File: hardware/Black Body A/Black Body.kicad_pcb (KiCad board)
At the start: 2 copper layers, 52 x 53.8 mm, 36 parts, among them IC2 MCP96L00T-E_MX, J1 53307-2471, J2 Conn_01x02, J3 Conn_01x04, J5 Conn_02x04_Top_Bottom, J7 Conn_02x03_Top_Bottom

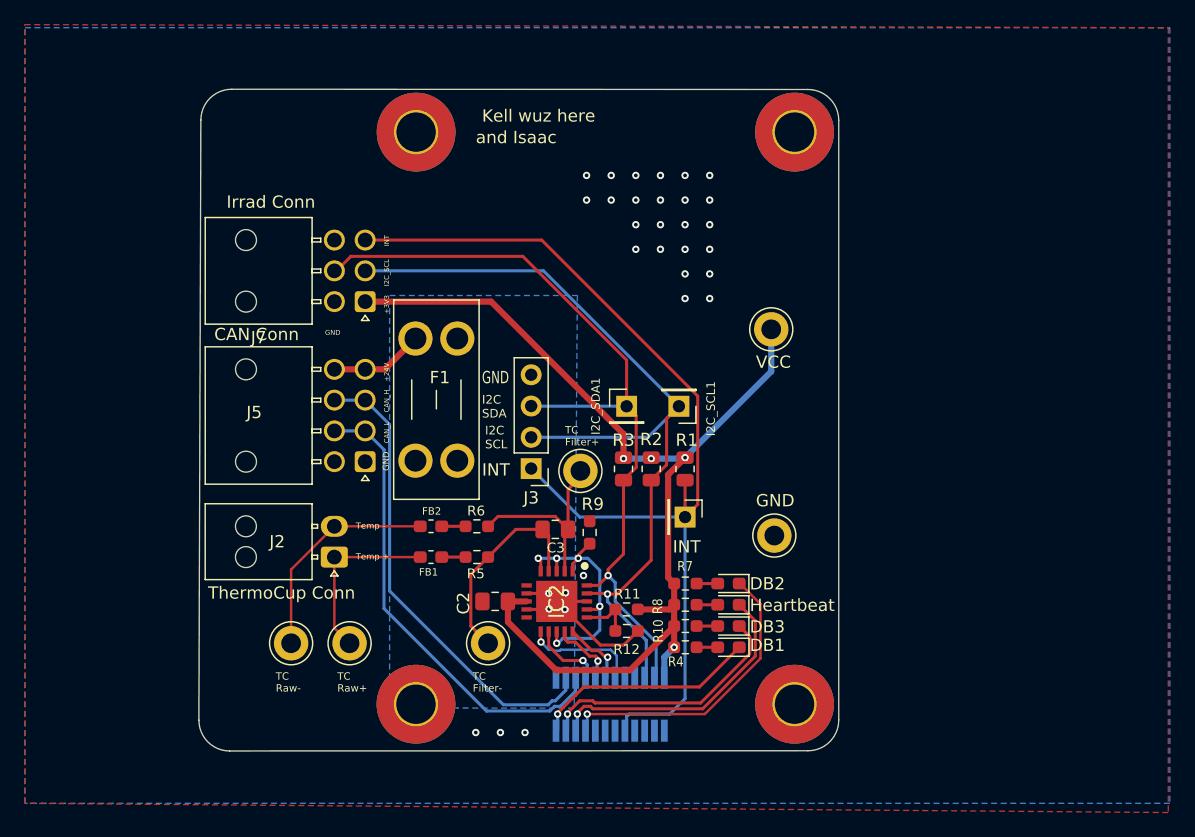
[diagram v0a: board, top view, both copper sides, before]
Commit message: updated irrad board layout + removed testpoints
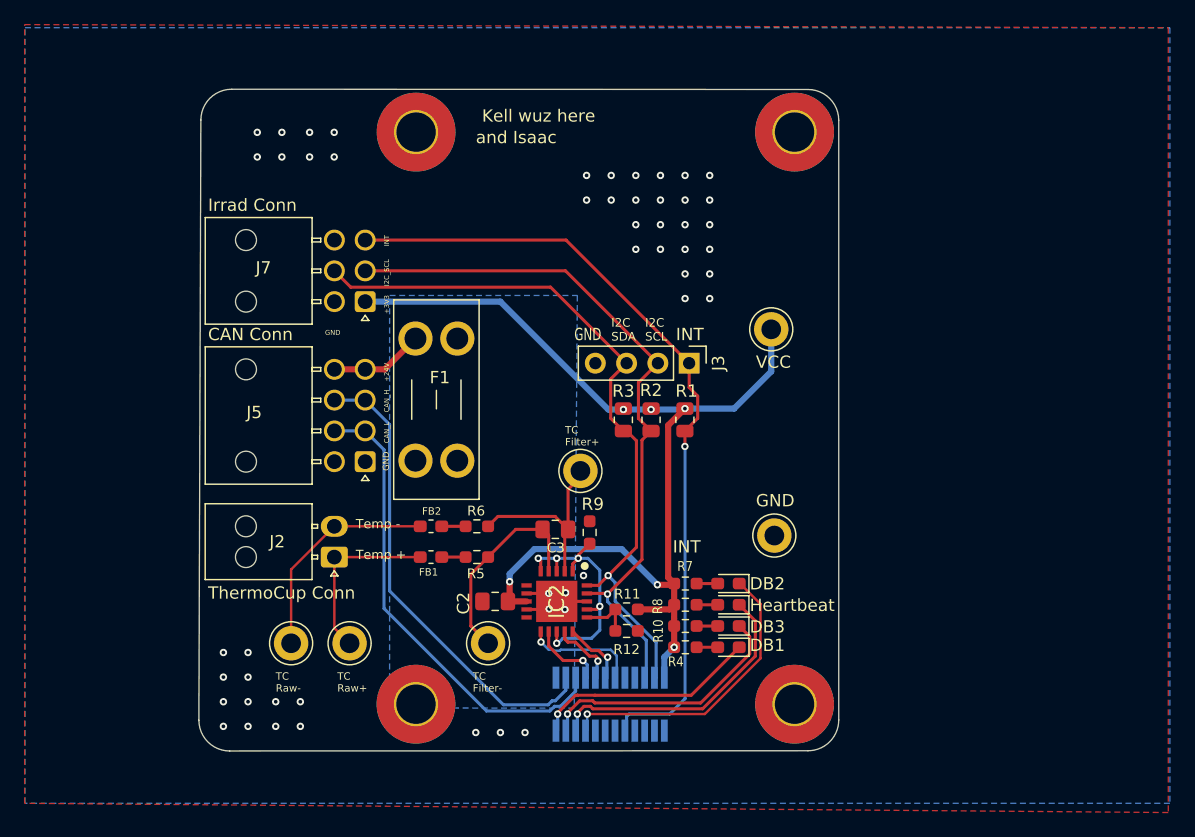
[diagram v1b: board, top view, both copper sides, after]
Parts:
- removed I2C_SCL1, I2C_SDA1, INT1: TestPoint, Connector_PinHeader_2.54mm:PinHeader_1x01_P2.54mm_Vertical
- moved J3 15.4 mm to (117.3, 89.2), turned to -90 degrees
- moved R1 3.99 mm to (117.0, 93.9)
- moved R2 3.99 mm to (114.2, 93.9)
- moved R3 3.99 mm to (112.0, 93.9)
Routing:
- net /INT: track 80.9 -> 64.9 mm, vias 0 -> 1
- net /I2C1_SCL: track 71.6 -> 58.0 mm
- net /I2C1_SDA: track 66.8 -> 59.0 mm
- net GND: track 15.8 -> 8.22 mm, vias 32 -> 52
- net +3V3: track 87.6 -> 86.6 mm, vias 4 -> 6

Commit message: updated 24Va
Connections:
- F2 pad 1: +24V -> /+24V_Ext
- J5 pad 1: +24V -> /+24V_Ext
- J5 pad 5: +24V -> /+24V_Ext
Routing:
- net +24V: track 7.62 -> 0.00 mm
- net GND: track 8.22 -> 14.3 mm, vias 52 -> 51
- added copper zone on B.Cu, net /+24V_Ext
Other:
- board text added: "and Isaac and Aarav and Frank"
- board text removed: "and Isaac"
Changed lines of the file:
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@@
 	(net 46 "/Temp-")
 	(net 47 "unconnected-(J7-Pin_6-Pad6)")
+	(net 48 "/+24V_Ext")
 	(footprint "Resistor_SMD:R_0603_1608Metric_Pad0.98x0.95mm_HandSolder"
 		(layer "F.Cu")
@@
 			(layers "*.Cu" "*.Mask")
 			(remove_unused_layers no)
-			(net 40 "+24V")
+			(net 48 "/+24V_Ext")
 			(pintype "passive")
 		)
@@
 			(layers "*.Cu" "*.Mask")
 			(remove_unused_layers no)
-			(net 40 "+24V")
+			(net 48 "/+24V_Ext")
 			(pintype "passive")
 		)
@@
 			(layers "*.Cu" "*.Mask")
 			(remove_unused_layers no)
-			(net 40 "+24V")
+			(net 48 "/+24V_Ext")
 			(pinfunction "Pin_1")
 			(pintype "passive")
@@
 			(layers "*.Cu" "*.Mask")
 			(remove_unused_layers no)
-			(net 40 "+24V")
+			(net 48 "/+24V_Ext")
 			(pinfunction "Pin_5")
 			(pintype "passive")
@@
 		)
 	)
-	(gr_text "and Isaac"
-		(at 100 71.5 0)
+	(gr_text "and Isaac and Aarav and Frank"
+		(at 100.1 71.6 0)
 		(layer "F.SilkS")
 		(effects
 			(font
-				(size 1 1)
+				(size 1 0.75)
 				(thickness 0.15)
 			)
@@
 		)
 	)
-	(gr_text "DB2"
-		(at 122.25 107.75 0)
+	(gr_text "DB1"
+		(at 122.3 107.8 0)
 		(layer "F.SilkS")
 		(effects
@@
 		)
 	)
-	(gr_text "DB3"
+	(gr_text "DB2"
 		(at 122.25 111.25 0)
 		(layer "F.SilkS")
@@
 	)
 	(gr_text "Kell wuz here"
-		(at 100.5 69.75 0)
+		(at 100.2 70.1 0)
 		(layer "F.SilkS")
 		(effects
@@
 		)
 	)
-	(gr_text "DB1\n"
+	(gr_text "DB3\n"
 		(at 122.25 112.75 0)
 		(layer "F.SilkS")
@@
 		)
 	)
-	(gr_text "INT"
-		(at 116 104.75 0)
-		(layer "F.SilkS")
-		(effects
-			(font
-				(size 1 1)
-				(thickness 0.1)
-			)
-			(justify left bottom)
-		)
-	)
 	(gr_text "I2C_SCL\n"
 		(at 93 83 90)
@@
 		(effects
 			(font
-				(size 1 1)
+				(size 1 0.75)
 				(thickness 0.15)
 			)
@@
 	)
 	(segment
+		(start 106.6 108.6)
+		(end 108.75 110.75)
+		(width 0.25)
+		(layer "F.Cu")
+		(net 1)
+	)
+	(segment
+		(start 106.575 108.6)
+		(end 106.65 108.6)
+		(width 0.25)
+		(layer "F.Cu")
+		(net 1)
+	)
+	(segment
 		(start 104.125 109.25)
 		(end 105.925 109.25)
@@
 	)
 	(segment
+		(start 106.65 108.6)
+		(end 108.75 106.5)
+		(width 0.25)
+		(layer "F.Cu")
+		(net 1)
+	)
+	(segment
 		(start 106.575 108.6)
 		(end 106.6 108.6)
@@
 	)
 	(via
-		(at 108.75 106.5)
-		(size 0.6)
-		(drill 0.3)
-		(layers "F.Cu" "B.Cu")
-		(net 1)
-	)
-	(via
 		(at 83.75 116.75)
 		(size 0.6)
@@
 	)
 	(segment
-		(start 88.515 89.75)
-		(end 91.015 89.75)
-		(width 0.5)
-		(layer "F.Cu")
-		(net 40)
-	)
-	(segment
-		(start 92.6 89.75)
-		(end 95.1 87.25)
-		(width 0.5)
-		(layer "F.Cu")
-		(net 40)
-	)
-	(segment
-		(start 91.015 89.75)
-		(end 92.6 89.75)
-		(width 0.5)
-		(layer "F.Cu")
-		(net 40)
-	)
-	(segment
 		(start 117.9375 112.325)
 		(end 119.65 112.325)
@@
 	)
 	(zone
+		(net 48)
+		(net_name "/+24V_Ext")
+		(layer "B.Cu")
+		(hatch edge 0.5)
+		(priority 2)
+		(connect_pads yes
+			(clearance 0.5)
+		)
+		(min_thickness 0.25)
+		(filled_areas_thickness no)
+		(fill yes
+			(thermal_gap 0.5)
+			(thermal_bridge_width 0.5)
+		)
+		(polygon
+			(pts
+				(xy 108.209939 85.11449) (xy 108.155686 92.275918) (xy 86.530023 92.243247) (xy 86.530023 85.11449)
+			)
+		)
+	)
+	(zone
 		(net 1)
 		(net_name "GND")
@@
 		(polygon
 			(pts
-				(xy 108.25 83.75) (xy 107.996041 117.272656) (xy 93 117.25) (xy 93 83.75)
+				(xy 108.183712 92.5) (xy 107.996041 117.272656) (xy 93 117.25) (xy 93 92.5)
 			)
 		)

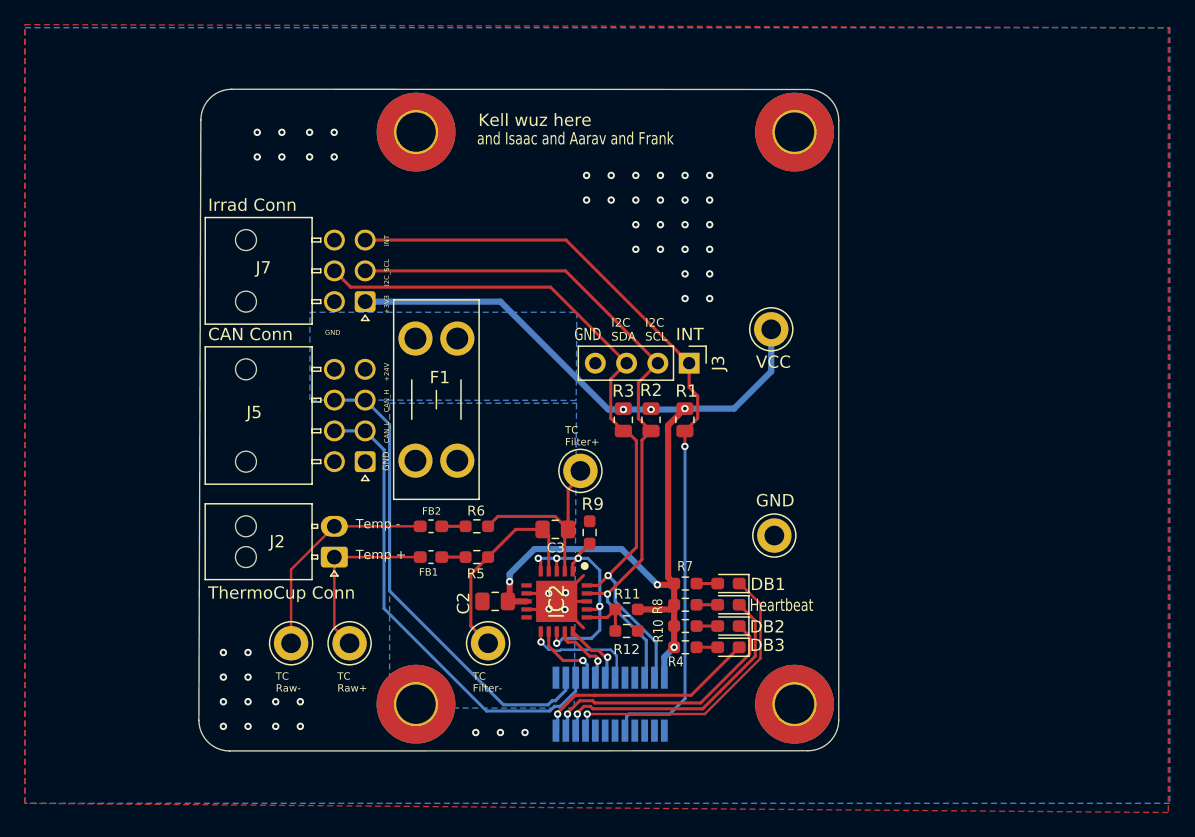
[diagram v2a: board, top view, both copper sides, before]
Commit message: added logic analyzer + LEDS
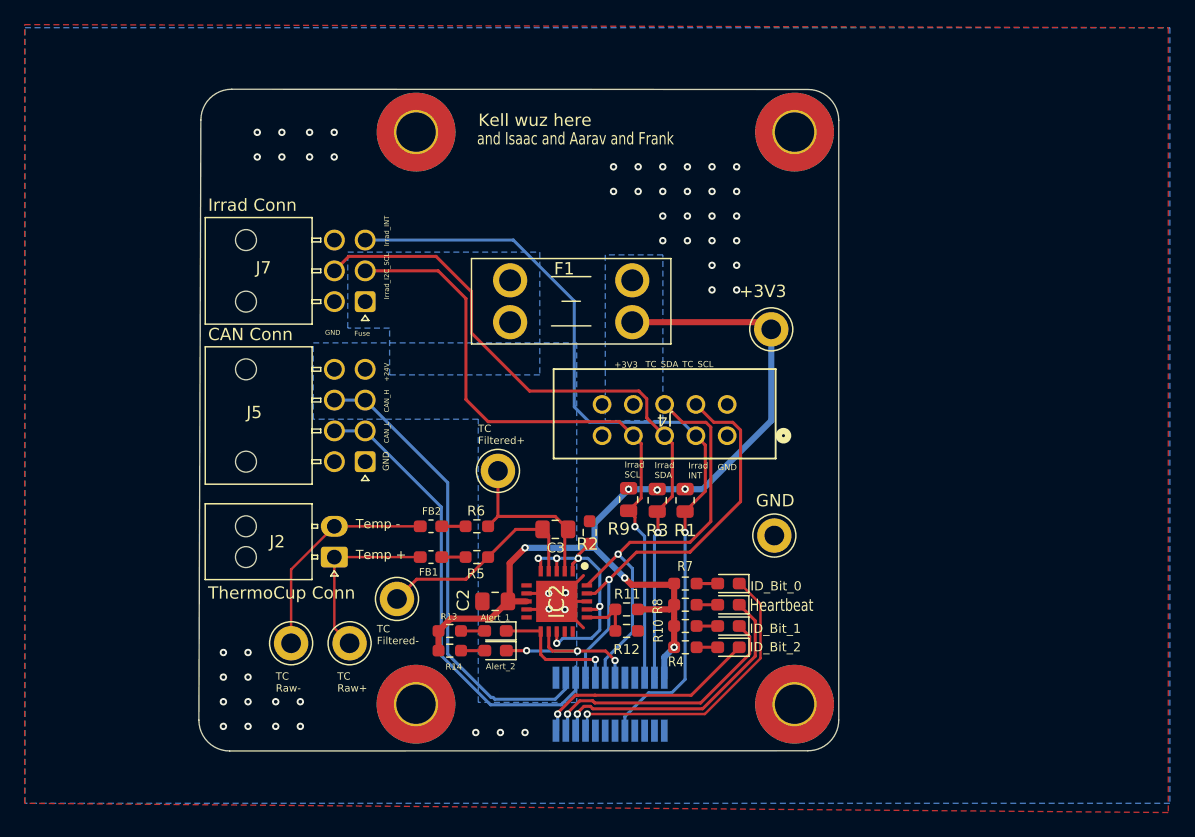
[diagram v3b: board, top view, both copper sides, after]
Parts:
- removed J3: Conn_01x04, Connector_PinHeader_2.54mm:PinHeader_1x04_P2.54mm_Vertical
- added Alert_1: LED, LED_SMD:LED_0603_1608Metric_Pad1.05x0.95mm_HandSolder, F.Cu at (101.6, 111.0)
- added Alert_2: LED, LED_SMD:LED_0603_1608Metric_Pad1.05x0.95mm_HandSolder, F.Cu at (101.6, 112.6)
- added J4: LogicAnalyzer, utsvt_connectors:CONN_SFH11-xxxC-D05-ST-XX_SUL, F.Cu at (120.4, 95.1)
- added R13: 1k, Resistor_SMD:R_0603_1608Metric_Pad0.98x0.95mm_HandSolder, F.Cu at (97.9, 111.0)
- added R14: 1k, Resistor_SMD:R_0603_1608Metric_Pad0.98x0.95mm_HandSolder, F.Cu at (97.9, 112.6)
- J1: footprint UTSVT-Conn:PeripheralSOM -> utsvt_connectors:PeripheralSOM
- R2, R3: value 1.5k -> 10k
- moved TP_TC_F_1 8.23 mm to (93.6, 108.4)
- moved R3 7.09 mm to (114.7, 100.4)
- moved R2 6.73 mm to (112.4, 100.3)
- moved TP_TC_F_2 6.70 mm to (101.8, 98.0)
- moved R1 6.54 mm to (117.0, 100.4)
- moved F2 6.39 mm to (102.8, 82.5), turned to 0 degrees
- renumbered DB_1 to ID_Bit_0, DB_2 to ID_Bit_1, DB_3 to ID_Bit_2
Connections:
- net /DB_Conn_1 renamed /ID_Bit_0
- net /DB_Conn_2 renamed /ID_Bit_1
- net /DB_Conn_3 renamed /ID_Bit_2
- net /INT renamed /Irrad_INT
- F2 pad 1: /+24V_Ext -> Net-(J7-Pin_1)
- F2 pad 2: +24V -> +3V3
- IC2 pad 14: /Alert_3 -> unconnected-(IC2-ALERT_3-Pad14)
- IC2 pad 15: /Alert_4 -> unconnected-(IC2-ALERT_4-Pad15)
- IC2 pad 19: /I2C1_SCL -> /TC_I2C_SCL
- IC2 pad 20: /I2C1_SDA -> /TC_I2C_SDA
- J1 pad 12: /Alert_1 -> /Alert_2
- J1 pad 14: /Alert_4 -> /TC_I2C_SDA
- J1 pad 16: /Alert_3 -> /Alert_1
- J1 pad 18: /Alert_2 -> /TC_I2C_SCL
- J1 pad 4: /I2C1_SDA -> /Irrad_I2C_SDA
- J1 pad 6: /I2C1_SCL -> /Irrad_I2C_SCL
- J5 pad 1: /+24V_Ext -> +24V
- J5 pad 5: /+24V_Ext -> +24V
- J7 pad 1: +3V3 -> Net-(J7-Pin_1)
- J7 pad 2: /I2C1_SCL -> /Irrad_I2C_SCL
- J7 pad 5: /I2C1_SDA -> /Irrad_I2C_SDA
- R2 pad 2: /I2C1_SCL -> /Irrad_I2C_SCL
- R3 pad 2: /I2C1_SDA -> /Irrad_I2C_SDA
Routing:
- net /I2C1_SDA: track 59.0 -> 0.00 mm, vias 1 -> 0
- net /I2C1_SCL: track 58.0 -> 0.00 mm, vias 1 -> 0
- net /Irrad_I2C_SDA: track 0.00 -> 57.6 mm, vias 0 -> 1
- net /Irrad_I2C_SCL: track 0.00 -> 53.0 mm, vias 0 -> 1
- net /TC_I2C_SDA: track 0.00 -> 35.8 mm, vias 0 -> 1
- net /TC_I2C_SCL: track 0.00 -> 34.7 mm, vias 0 -> 1
- net /Alert_2: track 6.06 -> 14.5 mm, vias 1 -> 3
- net +3V3: track 86.6 -> 78.2 mm
- net /Alert_3: track 5.56 -> 0.00 mm, vias 1 -> 0
- net /Alert_4: track 5.40 -> 0.00 mm, vias 1 -> 0
- net Net-(Alert_1-A): track 0.00 -> 1.92 mm
- net Net-(Alert_2-A): track 0.00 -> 1.73 mm
- net Net-(IC2-VIN+): track 16.2 -> 14.5 mm
- net /Irrad_INT: track 64.9 -> 66.6 mm
- net /Alert_1: track 9.39 -> 10.8 mm
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- added copper zone on B.Cu, net +3V3
- added copper zone on B.Cu, net Net-(J7-Pin_1)
- removed copper zone on B.Cu, net /+24V_Ext
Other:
- board text added: "Fuse"
- board text added: "ID_Bit_0"
- board text added: "ID_Bit_1"
- board text added: "ID_Bit_2"
- board text added: "Irrad INT"
- board text added: "Irrad SCL"
- board text added: "Irrad SDA"
- board text added: "Irrad_I2C_SCL"
- board text added: "Irrad_I2C_SDA"
- board text added: "Irrad_INT"
- board text added: "TC Filtered+"
- board text added: "TC Filtered-"
- board text added: "TC_SCL"
- board text added: "TC_SDA"
- board text removed: "DB1"
- board text removed: "DB2"
- board text removed: "DB3"
- board text removed: "I2C SCL"
- board text removed: "I2C SDA"
- board text removed: "I2C_SCL"
- board text removed: "I2C_SDA"
- board text removed: "INT"
- board text removed: "TC Filter+"
- board text removed: "TC Filter-"
- board text removed: "VCC"
